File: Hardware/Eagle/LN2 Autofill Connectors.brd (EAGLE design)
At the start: 114.3 x 69.8 mm, 45 parts, among them J1 Phoenix 1455997, J2 Phoenix 1455997, J3 Phoenix 1455997, J4 Phoenix 1455997, J5 Phoenix 1456116, J6 Phoenix 1456116, J7 Phoenix 1456116, J8 Phoenix 1456116, Q1 RTR030N05HZG, Q2 RTR030N05HZG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

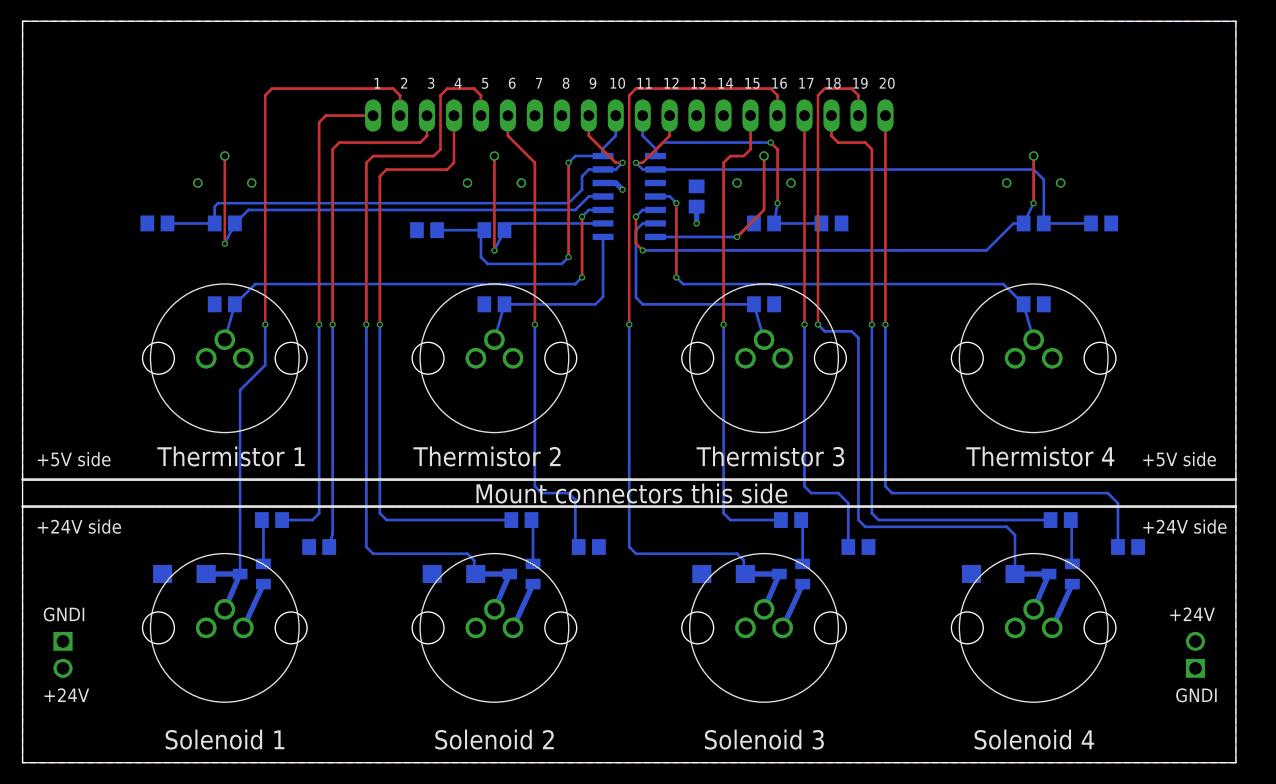
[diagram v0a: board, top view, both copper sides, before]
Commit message: Added gate resistor and re-routed connector board
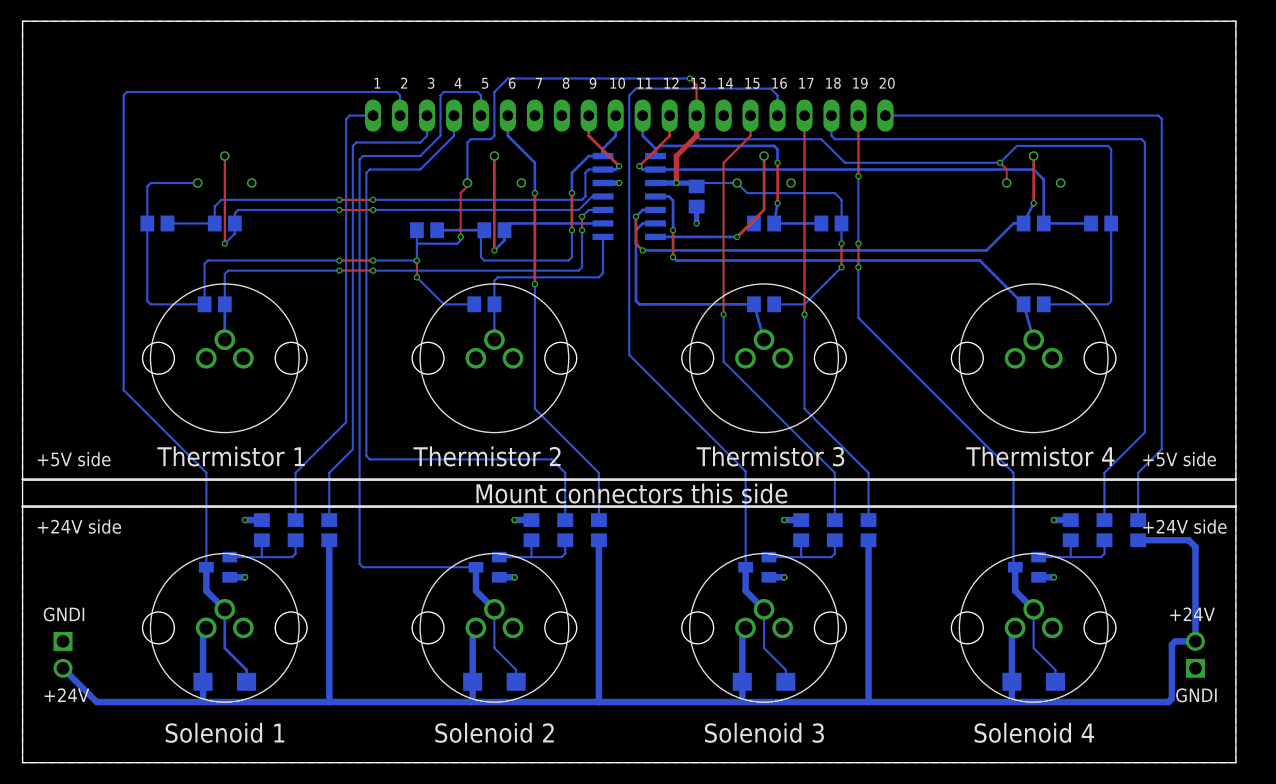
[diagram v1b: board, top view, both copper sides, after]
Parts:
- added R25, R26, R27, R28: 100K, AUmlib:R0805
- JP2, JP3: value (none) -> MOLEX 53822112022
- moved D2 10.9 mm to (44.5, 7.62)
- moved D4 10.9 mm to (95.2, 7.62)
- moved D1 10.9 mm to (19.1, 7.62)
- moved D3 10.9 mm to (69.8, 7.62)
- moved R18 4.24 mm to (51.1, 21.9), turned to 270 degrees
- moved R19 4.24 mm to (76.5, 21.9), turned to 270 degrees
- moved R20 4.24 mm to (101.9, 21.9), turned to 270 degrees
- moved Q4 3.24 mm to (94.6, 18.4)
- moved Q2 3.24 mm to (43.8, 18.4)
- moved Q1 3.24 mm to (18.4, 18.4)
- moved Q3 3.24 mm to (69.2, 18.4)
- moved R17 2.42 mm to (25.7, 21.9), turned to 270 degrees
- moved R23 1.85 mm to (79.7, 21.9), turned to 90 degrees
- moved R24 1.85 mm to (105.1, 21.9), turned to 90 degrees
- moved R21 1.85 mm to (28.9, 21.9), turned to 90 degrees
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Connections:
- net GNDI: now also R25.1, R26.1, R27.1, R28.1
- net N$1: now also R25.2
- net N$2: now also R26.2
- net N$3: now also R27.2
- net N$4: now also R28.2
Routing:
- net +5V: track 0.00 -> 205.4 mm, vias 0 -> 10
- net +24V: track 0.00 -> 202.3 mm
- net LED1-K: track 68.0 -> 88.2 mm, vias 1 -> 0
- net LED4-K: track 75.1 -> 61.0 mm, vias 1 -> 3
- net VALV4: track 57.6 -> 68.8 mm, vias 1 -> 0
- net GNDI: track 18.2 -> 12.1 mm, vias 0 -> 8
- net LED2-K: track 73.9 -> 79.9 mm, vias 1 -> 0
- net VALV2: track 56.4 -> 62.1 mm, vias 1 -> 0
- net N$1: track 4.19 -> 9.20 mm
- net N$3: track 4.19 -> 9.20 mm
- net N$2: track 4.19 -> 9.20 mm
- net N$4: track 4.25 -> 9.20 mm
- net VALV1: track 45.9 -> 42.4 mm, vias 1 -> 0
- net LED1-A: track 48.8 -> 45.5 mm, vias 1 -> 0
- net LED4-A: track 61.6 -> 64.9 mm, vias 1 -> 0
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- removed copper zone on layer 16, net +24V
- removed copper zone on layer 16, net +5V
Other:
- board text added: "BOSS LN2 Autofill Connectors 2021-02-21"
- board text removed: "BOSS LN2 Autofill Connectors 2020-03-07"

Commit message: Brought in test code developed in a different directory
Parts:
- R21, R22: value 47K -> 1.5K
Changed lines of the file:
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@@
 <drawing>
 <settings>
-<setting alwaysvectorfont="yes"/>
+<setting alwaysvectorfont="no"/>
 <setting verticaltext="up"/>
 </settings>
@@
 <attribute name="NAME" x="104.4575" y="9.2075" size="1.27" layer="26" font="vector" rot="MR180"/>
 </element>
-<element name="R21" library="AUmlib" library_urn="urn:adsk.eagle:library:9166017" package="R0805" package3d_urn="urn:adsk.eagle:package:4021199/4" value="47K" x="28.8925" y="21.9075" smashed="yes" rot="MR90">
+<element name="R21" library="AUmlib" library_urn="urn:adsk.eagle:library:9166017" package="R0805" package3d_urn="urn:adsk.eagle:package:4021199/4" value="1.5K" x="28.8925" y="21.9075" smashed="yes" rot="MR90">
 <attribute name="NAME" x="28.2575" y="16.1925" size="1.27" layer="26" font="vector" rot="MR90"/>
 <attribute name="SPICEPREFIX" value="R" x="28.8925" y="21.9075" size="1.778" layer="28" rot="MR90" display="off"/>
 </element>
-<element name="R22" library="AUmlib" library_urn="urn:adsk.eagle:library:9166017" package="R0805" package3d_urn="urn:adsk.eagle:package:4021199/4" value="47K" x="54.2925" y="21.9075" smashed="yes" rot="MR90">
+<element name="R22" library="AUmlib" library_urn="urn:adsk.eagle:library:9166017" package="R0805" package3d_urn="urn:adsk.eagle:package:4021199/4" value="1.5K" x="54.2925" y="21.9075" smashed="yes" rot="MR90">
 <attribute name="NAME" x="53.6575" y="16.1925" size="1.27" layer="26" font="vector" rot="MR90"/>
 <attribute name="SPICEPREFIX" value="R" x="54.2925" y="21.9075" size="1.778" layer="28" rot="MR90" display="off"/>
